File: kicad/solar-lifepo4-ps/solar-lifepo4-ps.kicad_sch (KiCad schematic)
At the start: 29 parts, among them J1 Screw_Terminal_01x02, T1 SI4435DY, U1 CN3722

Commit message: still WIP
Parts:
- added BAT1: ~, foxisfrickellibrary:batteryholder_keystone_1106, symbol foxisfrickellibrary:batteryholder_keystone_1106_1x_26650
- added C11: 100nF, Capacitor_SMD:C_0402_1005Metric, symbol Device:C
- added R11: 100, Resistor_SMD:R_0805_2012Metric, symbol Device:R
- added R2: 1.8k, Resistor_SMD:R_0603_1608Metric, symbol Device:R
- added T2, T3: AO3400A, Package_TO_SOT_SMD:SOT-23, symbol Transistor_FET:AO3400A
- added U2: HY2112, Package_TO_SOT_SMD:SOT-23-6, symbol foxisfrickellibrary:HY2112
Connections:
- net GND: now also R2.2, T3.2 (S)
- net VBATCHG+ renamed VBAT+
- net VBAT+: now also BAT1.1 (+), R11.2
- new net: T2.1 (G), U2.1 (OD)
- new net: T2.3 (D), T3.3 (D)
- new net: C11.2, R11.1, U2.5 (VDD)
- new net: T3.1 (G), U2.3 (OC)
- new net: R2.1, U2.2 (CS)
- new net VBAT-: BAT1.2 (-), C11.1, T2.2 (S), U2.6 (GND)

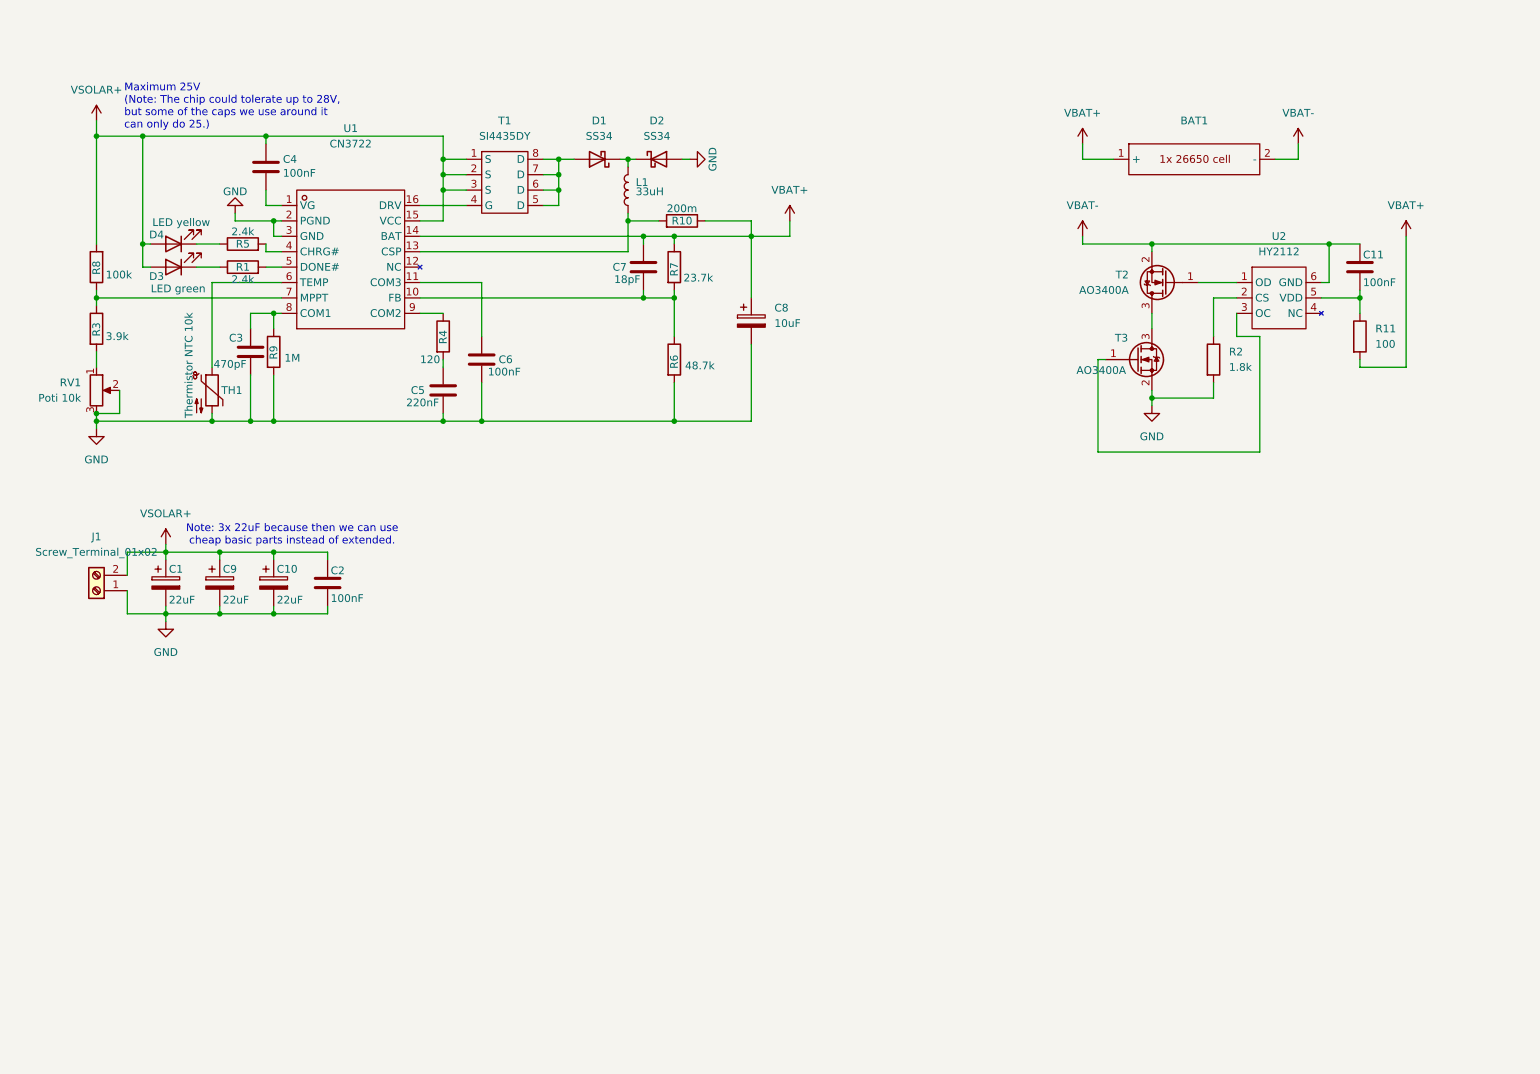
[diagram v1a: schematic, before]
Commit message: current state. All the main circuit has been designed now. TODO: voltage divider output to permit a connected MC to measure voltages; fix square hole in PCB because JLCPCB will not be able to manufacture that, we need to round the edges.
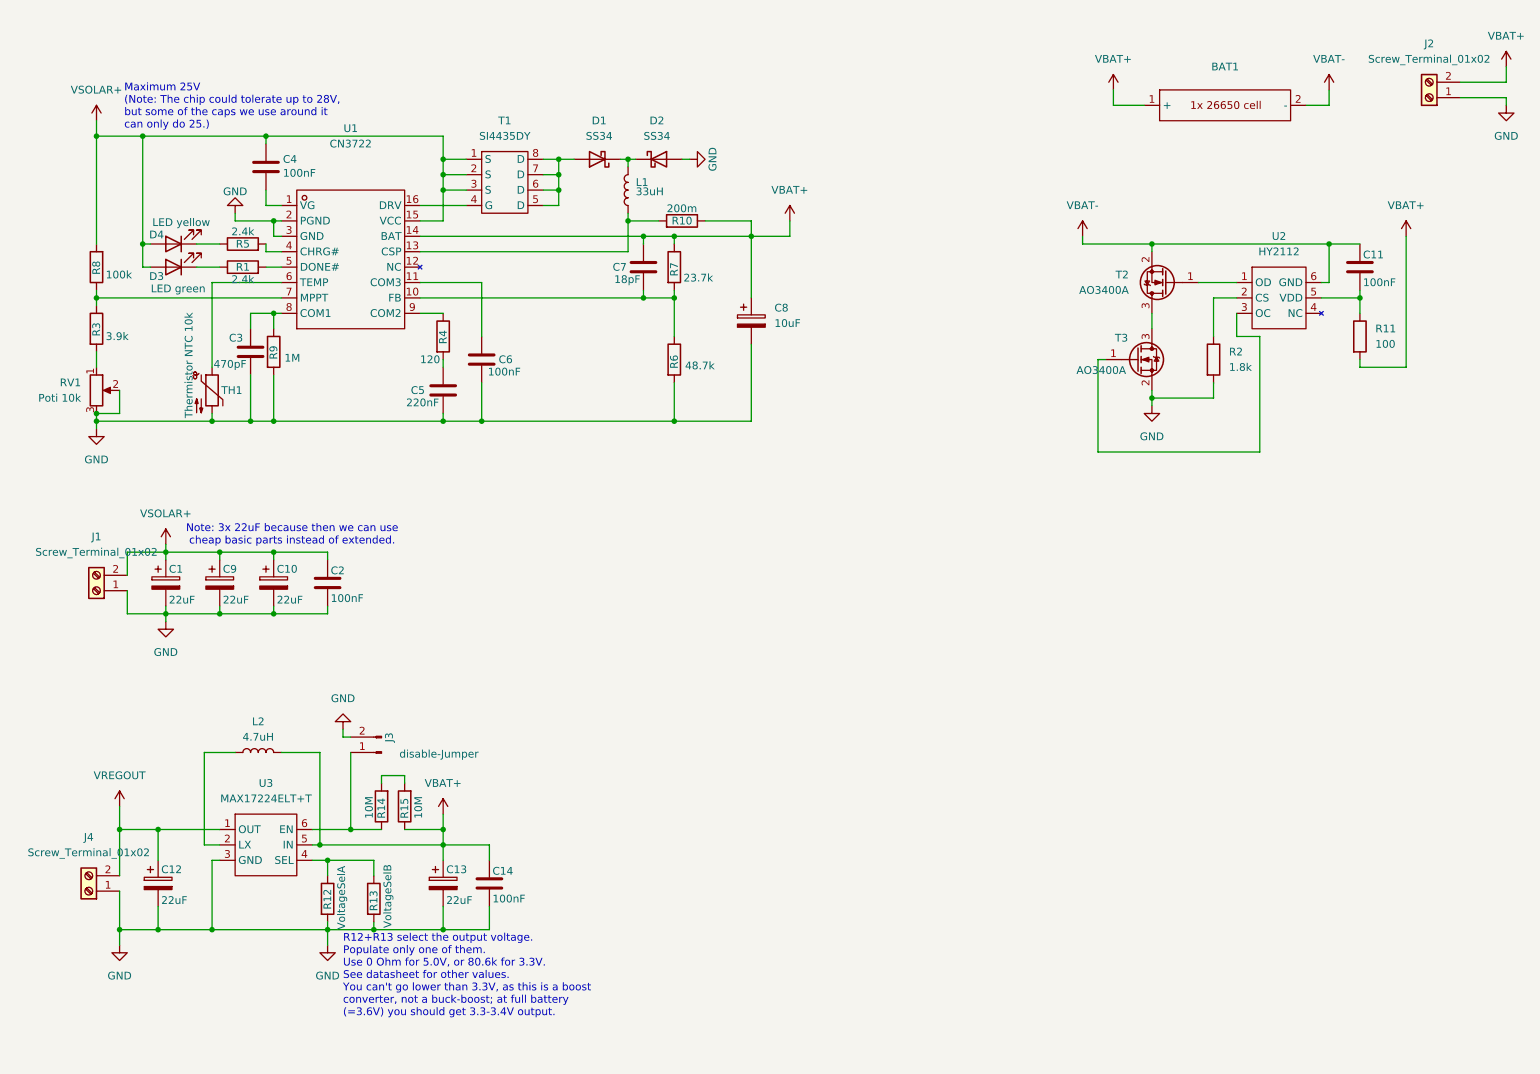
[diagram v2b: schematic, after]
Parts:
- added C12, C13: 22uF, Capacitor_SMD:C_0805_2012Metric, symbol Device:C_Polarized
- added C14: 100nF, Capacitor_SMD:C_0402_1005Metric, symbol Device:C
- added J2, J4: Screw_Terminal_01x02, TerminalBlock_MetzConnect:TerminalBlock_MetzConnect_Type073_RT02602HBLU_1x02_P5.08mm_Horizontal, symbol Connector:Screw_Terminal_01x02
- added J3: disable-Jumper, Connector_PinSocket_2.54mm:PinSocket_1x02_P2.54mm_Vertical, symbol Connector:Conn_01x02_Pin
- added L2: 4.7uH, Inductor_SMD:L_Sunlord_MWSA0603S, symbol Device:L
- added R12: VoltageSelA, Resistor_THT:R_Axial_DIN0207_L6.3mm_D2.5mm_P10.16mm_Horizontal, symbol Device:R
- added R13: VoltageSelB, Resistor_SMD:R_1206_3216Metric, symbol Device:R
- added R14, R15: 10M, Resistor_SMD:R_0603_1608Metric, symbol Device:R
- added U3: MAX17224ELT+T, foxisfrickellibrary:UDFN-6_L2.0-W2.0-P0.65-BL-1, symbol foxisfrickellibrary:MAX1722x
- BAT1: now left out of the parts list
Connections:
- net GND: now also C12.2, C13.2, C14.2, J2.1 (Pin_1), J3.2 (Pin_2), J4.1 (Pin_1), R12.2, R13.2, U3.3 (GND)
- net VBAT+: now also C13.1, C14.1, J2.2 (Pin_2), L2.2, R15.1, U3.5 (IN)
- new net: R12.1, R13.1, U3.4 (SEL)
- new net: L2.1, U3.2 (LX)
- new net: J3.1 (Pin_1), R14.1, U3.6 (EN)
- new net: R14.2, R15.2
- new net VREGOUT: C12.1, J4.2 (Pin_2), U3.1 (OUT)
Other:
- note added: "R12+R13 select the output voltage. Populate only one of them. Use 0 Ohm for 5.0V, or 80.6k for 3.3V. See datasheet for other values. You can't go lower than 3.3V, as this is a boost converter, not a buck-boost; at full battery (=3.6V) you should get 3.3-3.4V output."
- moved on the sheet: BAT1

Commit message: rev 0, as it was sent to jlcpcb for production.
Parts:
- added C15, C16: 1nF, Capacitor_SMD:C_0603_1608Metric, symbol Device:C
- added J5: SenseVBAT, Connector_PinHeader_2.54mm:PinHeader_1x01_P2.54mm_Vertical, symbol Connector:Conn_01x01_Pin
- added J6: SenseVSOLAR, Connector_PinHeader_2.54mm:PinHeader_1x01_P2.54mm_Vertical, symbol Connector:Conn_01x01_Pin
- added R16, R17, R19: 10M, Resistor_SMD:R_0603_1608Metric, symbol Device:R
- added R18: 1M, Resistor_SMD:R_0402_1005Metric, symbol Device:R
- BAT1: footprint foxisfrickellibrary:batteryholder_keystone_1106 -> foxisfrickellibrary:batteryholder_keystone_1106-jlcpcb
- J4: renamed from J3; footprint Connector_PinSocket_2.54mm:PinSocket_1x02_P2.54mm_Vertical -> Connector_PinHeader_2.54mm:PinHeader_1x02_P2.54mm_Vertical
- renumbered J4 to J3
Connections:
- net GND: now also C15.2, C16.2, R17.2, R18.2
- net VBAT+: now also R16.1
- net VSOLAR+: now also R19.1
- new net: C16.1, J5.1 (Pin_1), R16.2, R17.1
- new net: C15.1, J6.1 (Pin_1), R18.1, R19.2
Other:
- note added: "Battery Protection Circuit"
- note added: "R12+R13 select the output voltage. Populate only one of them. Use 0 Ohm for 5.0V, or 80.6k for 3.3V, or 66.5k for 3.4V. See datasheet for other values. You can't go lower than 3.3V, as this is a boost converter, not a buck-boost; at full battery (=3.6V) the lowest it can produce is about 3.4V."
- note added: "Solar Charge Controller"
- note added: "Voltage Regulator / DC-DC Boost Converter"
- note removed: "R12+R13 select the output voltage. Populate only one of them. Use 0 Ohm for 5.0V, or 80.6k for 3.3V. See datasheet for other values. You can't go lower than 3.3V, as this is a boost converter, not a buck-boost; at full battery (=3.6V) you should get 3.3-3.4V output."
- moved on the sheet: C12, C13, C14, C3, C4, C5, C6, C7, C8, D1, D2, D3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

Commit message: first few fixes after Rev. 0 arrived from the JLCPCB-fab. It seems to be mostly working fine, but I made a few small errors - like forgetting the labels for +/- and using resistor-footprints for the two LEDs
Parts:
- D3, D4: footprint Resistor_SMD:R_0805_2012Metric -> LED_SMD:LED_0805_2012Metric
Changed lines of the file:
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@@
 			)
 		)
-		(property "Footprint" "Resistor_SMD:R_0805_2012Metric"
+		(property "Footprint" "LED_SMD:LED_0805_2012Metric"
 			(at 43.18 53.34 0)
 			(effects
@@
 			)
 		)
-		(property "Footprint" "Resistor_SMD:R_0805_2012Metric"
+		(property "Footprint" "LED_SMD:LED_0805_2012Metric"
 			(at 43.18 57.15 0)
 			(effects

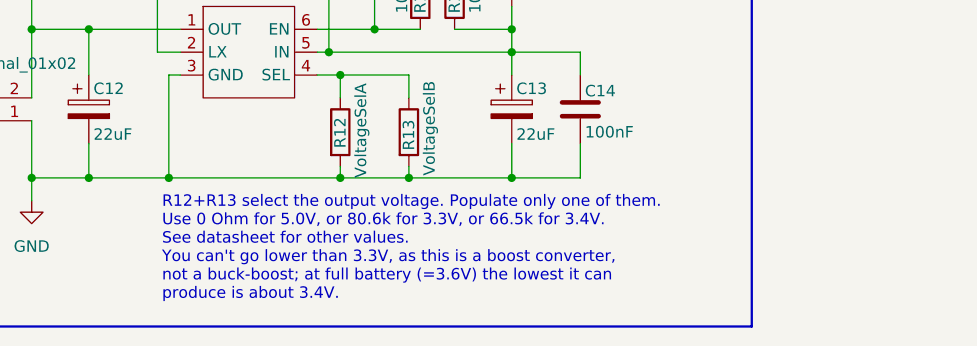
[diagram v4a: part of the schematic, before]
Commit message: more labeling on the silkscreen, minor ground plane movement.
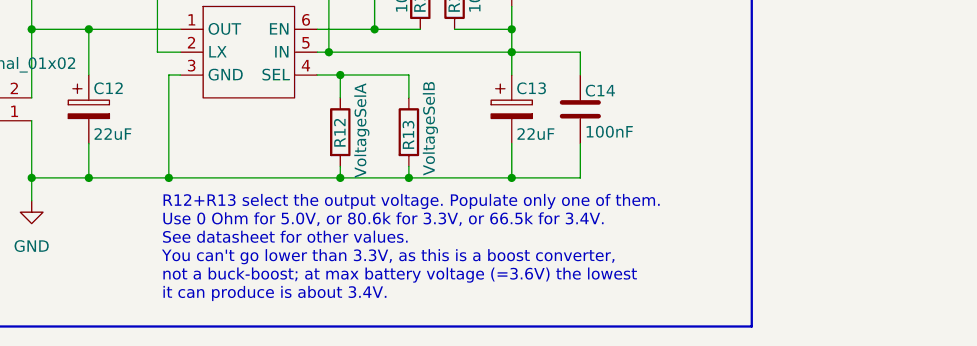
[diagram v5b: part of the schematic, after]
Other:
- note added: "R12+R13 select the output voltage. Populate only one of them. Use 0 Ohm for 5.0V, or 80.6k for 3.3V, or 66.5k for 3.4V. See datasheet for other values. You can't go lower than 3.3V, as this is a boost converter, not a buck-boost; at max battery voltage (=3.6V) the lowest it can produce is about 3.4V."
- note removed: "R12+R13 select the output voltage. Populate only one of them. Use 0 Ohm for 5.0V, or 80.6k for 3.3V, or 66.5k for 3.4V. See datasheet for other values. You can't go lower than 3.3V, as this is a boost converter, not a buck-boost; at full battery (=3.6V) the lowest it can produce is about 3.4V."
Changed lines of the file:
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@@
 		)
 	)
-	(text "R12+R13 select the output voltage. Populate only one of them.\nUse 0 Ohm for 5.0V, or 80.6k for 3.3V, or 66.5k for 3.4V.\nSee datasheet for other values.\nYou can't go lower than 3.3V, as this is a boost converter,\nnot a buck-boost; at full battery (=3.6V) the lowest it can\nproduce is about 3.4V.\n"
+	(text "R12+R13 select the output voltage. Populate only one of them.\nUse 0 Ohm for 5.0V, or 80.6k for 3.3V, or 66.5k for 3.4V.\nSee datasheet for other values.\nYou can't go lower than 3.3V, as this is a boost converter,\nnot a buck-boost; at max battery voltage (=3.6V) the lowest\nit can produce is about 3.4V.\n"
 		(exclude_from_sim no)
 		(at 52.578 181.864 0)

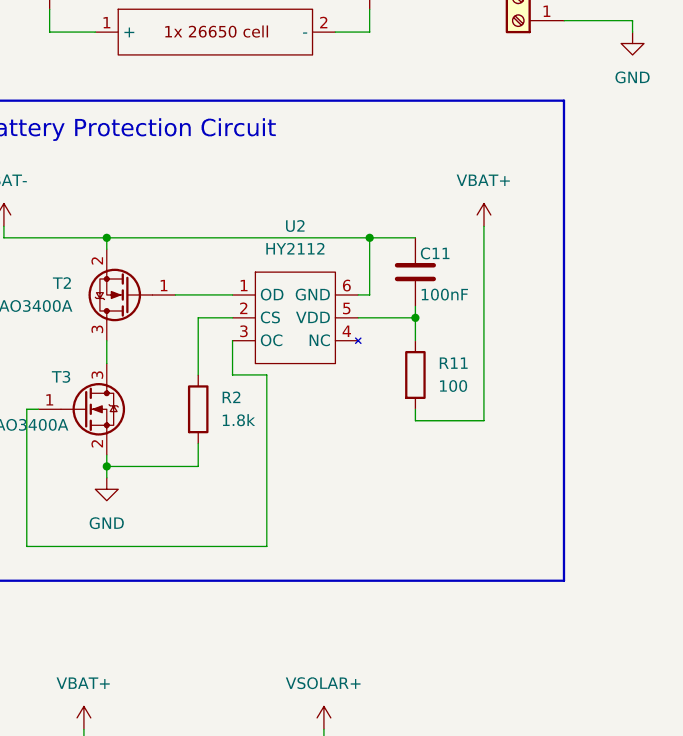
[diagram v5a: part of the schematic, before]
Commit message: add pushbutton to force the battery protection circuit into "normal" mode. When a battery is inserted, but there is not and has never been enough power to actually charge, the battery protection circuit may remain in a state where the output is turned off. Shorting pins 2+6 (by pressing this button) forces the battery protection IC back into "normal" mode, with output on.
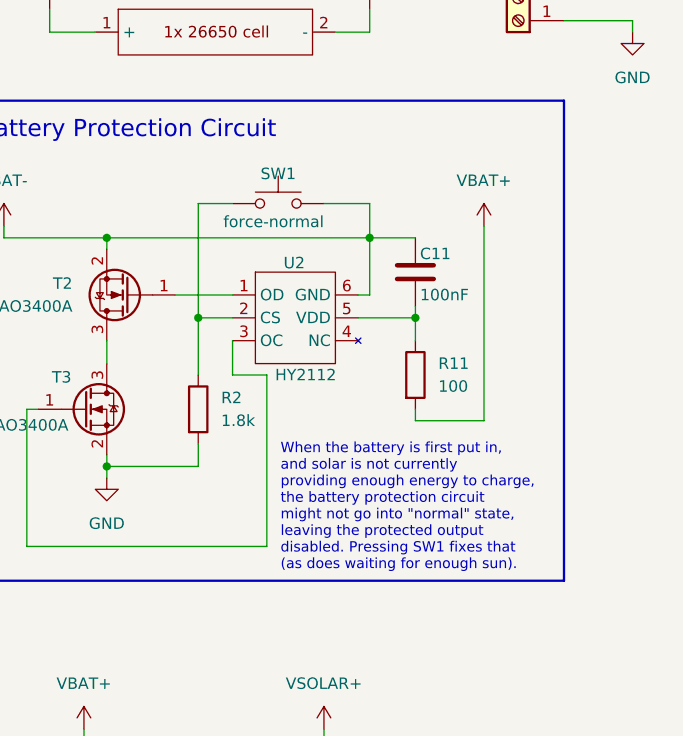
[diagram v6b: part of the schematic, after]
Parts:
- added SW1: force-normal, Button_Switch_SMD:SW_Push_1P1T_XKB_TS-1187A, symbol Switch:SW_Push
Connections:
- net VBAT-: now also SW1.2
- net at R2.1, U2.2 (CS): now also SW1.1
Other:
- note added: "When the battery is first put in, and solar is not currently providing enough energy to charge, the battery protection circuit might not go into "normal" state, leaving the protected output disabled. Pressing SW1 fixes that (as does waiting for enough sun)."
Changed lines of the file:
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@@
 	)
 	(junction
+		(at 209.55 64.77)
+		(diameter 0)
+		(color 0 0 0 0)
+	)
+	(junction
 		(at 91.44 160.02)
 		(diameter 0)
@@
 	(wire
 		(pts
+			(xy 209.55 52.07) (xy 213.36 52.07)
+		)
+		(stroke
+			(width 0)
+			(type default)
+		)
+	)
+	(wire
+		(pts
 			(xy 125.73 62.23) (xy 125.73 60.96)
 		)
@@
 	(wire
 		(pts
+			(xy 228.6 52.07) (xy 228.6 55.88)
+		)
+		(stroke
+			(width 0)
+			(type default)
+		)
+	)
+	(wire
+		(pts
 			(xy 59.69 82.55) (xy 87.63 82.55)
 		)
@@
 	(wire
 		(pts
+			(xy 223.52 52.07) (xy 228.6 52.07)
+		)
+		(stroke
+			(width 0)
+			(type default)
+		)
+	)
+	(wire
+		(pts
 			(xy 63.5 116.84) (xy 54.61 116.84)
 		)
@@
 	(wire
 		(pts
+			(xy 209.55 64.77) (xy 209.55 52.07)
+		)
+		(stroke
+			(width 0)
+			(type default)
+		)
+	)
+	(wire
+		(pts
 			(xy 91.44 162.56) (xy 91.44 160.02)
 		)
@@
 		)
 	)
+	(text "When the battery is first put in,\nand solar is not currently\nproviding enough energy to charge,\nthe battery protection circuit\nmight not go into \"normal\" state,\nleaving the protected output\ndisabled. Pressing SW1 fixes that\n(as does waiting for enough sun)."
+		(exclude_from_sim no)
+		(at 218.694 85.852 0)
+		(effects
+			(font
+				(size 1.143 1.143)
+			)
+			(justify left)
+		)
+	)
 	(symbol
 		(lib_id "power:GND")
@@
 	)
 	(symbol
+		(lib_id "Switch:SW_Push")
+		(at 218.44 52.07 0)
+		(unit 1)
+		(exclude_from_sim no)
+		(in_bom yes)
+		(on_board yes)
+		(dnp no)
+		(property "Reference" "SW1"
+			(at 218.44 48.768 0)
+			(effects
+				(font
+					(size 1.27 1.27)
+				)
+			)
+		)
+		(property "Value" "force-normal"
+			(at 217.932 54.102 0)
+			(effects
+				(font
+					(size 1.27 1.27)
+				)
+			)
+		)
+		(property "Footprint" "Button_Switch_SMD:SW_Push_1P1T_XKB_TS-1187A"
+			(at 218.44 46.99 0)
+			(effects
+				(font
+					(size 1.27 1.27)
+				)
+				(hide yes)
+			)
+		)
+		(property "Datasheet" "~"
+			(at 218.44 46.99 0)
+			(effects
+				(font
+					(size 1.27 1.27)
+				)
+				(hide yes)
+			)
+		)
+		(property "Description" "Push button switch, generic, two pins"
+			(at 218.44 52.07 0)
+			(effects
+				(font
+					(size 1.27 1.27)
+				)
+				(hide yes)
+			)
+		)
+		(pin "1"
+		)
+		(pin "2"
+		)
+		(instances
+			(project "solar-lifepo4-ps"
+				(path "/8d3797f9-5aa5-4ea9-98f2-af1f4fbf3757"
+					(reference "SW1")
+					(unit 1)
+				)
+			)
+		)
+	)
+	(symbol
 		(lib_id "Device:R")
 		(at 233.68 71.12 0)
@@
 		(on_board yes)
 		(dnp no)
-		(fields_autoplaced yes)
 		(property "Reference" "U2"
-			(at 220.345 54.61 0)
+			(at 220.218 58.674 0)
 			(effects
 				(font
@@
 		)
 		(property "Value" "HY2112"
-			(at 220.345 57.15 0)
+			(at 221.488 71.12 0)
 			(effects
 				(font

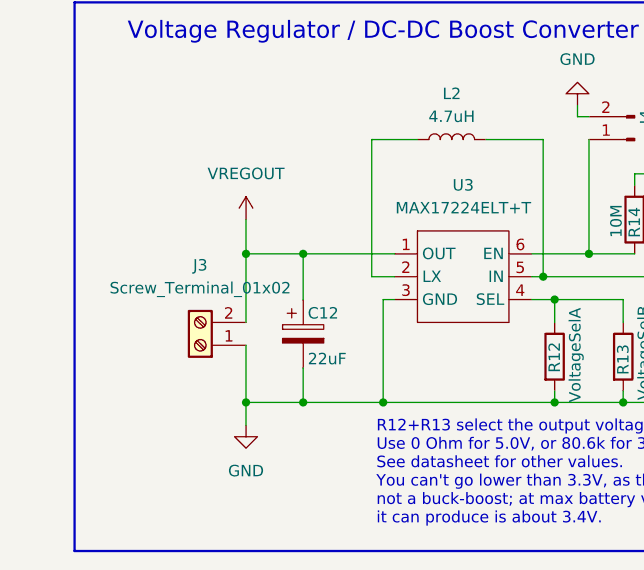
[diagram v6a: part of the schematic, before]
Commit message: add more capacitors at the output of the voltage converter because as it turns out, 1x 22uF was just NOT enough. So we now have 3x 22uF instead.
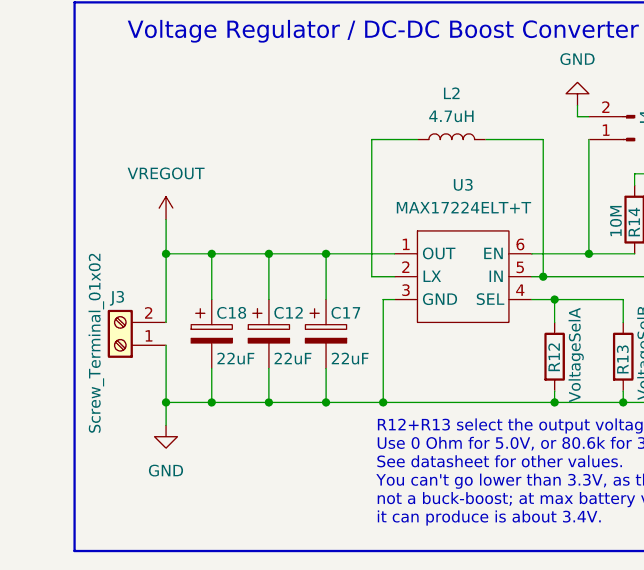
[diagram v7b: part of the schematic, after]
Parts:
- added C17, C18: 22uF, Capacitor_SMD:C_0805_2012Metric, symbol Device:C_Polarized
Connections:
- net GND: now also C17.2, C18.2
- net VREGOUT: now also C17.1, C18.1
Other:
- moved on the sheet: C12, J3
